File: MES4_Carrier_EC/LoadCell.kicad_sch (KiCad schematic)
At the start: 23 parts, among them J12 LC SIG, J13 LC EXC, U9 ADS1232IPWR

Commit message: Put relay coil feedback back on PA0-PA3 (MES4 GPIO standard)
All 14 module GPIOs now follow the MES4-CIF §2c table. The TCA9535 is
removed from the Relays 3-4 sheet and J1 fingers 43/45/47/49 drive the
relay 1-4 feedback dividers again. The winch relays are left undriven
(gate inputs no-connected, 100k pull-downs hold them off) until they
move to the TCA9535 + photoMOS design (HANDOFF.md step 2).

Removing U4 renumbers U5-U12 to U4-U11 and C15-C45 to C14-C44; the
README refs follow. Adds generator/checks.py (pin/pad, single-pin nets,
duplicate UUIDs, LCSC numbers), run by run.sh after ERC.

Co-Authored-By: Claude Opus 5.5 <noreply@anthropic.com>
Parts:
- removed C30: 100nF, Capacitor_SMD:C_0402_1005Metric, symbol Device:C
- removed R42: 100k, Resistor_SMD:R_0402_1005Metric, symbol Device:R
- removed U9: ADS1232IPWR, Package_SO:TSSOP-24_4.4x7.8mm_P0.65mm, symbol MES4-Carrier-EC:ADS1232IPW
- added C20: 10nF C0G, Capacitor_SMD:C_0402_1005Metric, symbol Device:C
- added R41: 100k, Resistor_SMD:R_0402_1005Metric, symbol Device:R
- added U8: ADS1232IPWR, Package_SO:TSSOP-24_4.4x7.8mm_P0.65mm, symbol MES4-Carrier-EC:ADS1232IPW
- C21, C24, C26: value 10nF C0G -> 100nF C0G; footprint Capacitor_SMD:C_0402_1005Metric -> Capacitor_SMD:C_1206_3216Metric; LCSC C3855387 -> C97946
- C22, C25: value 100nF C0G -> 10nF C0G; footprint Capacitor_SMD:C_1206_3216Metric -> Capacitor_SMD:C_0402_1005Metric; LCSC C97946 -> C3855387
- C27: value 100nF C0G -> 10uF 25V; footprint Capacitor_SMD:C_1206_3216Metric -> Capacitor_SMD:C_0805_2012Metric; LCSC C97946 -> C15850
- C28: value 10uF 25V -> 100nF; footprint Capacitor_SMD:C_0805_2012Metric -> Capacitor_SMD:C_0402_1005Metric; LCSC C15850 -> C1525
- renumbered R41 to R42
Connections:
- net +3V3_MOD: now also C29.1, U8.1 (DVDD), U8.19 (GAIN0), U8.20 (GAIN1)
- net GND: now also C22.2, C25.2, C27.2, C20.2, R41.2, U8.13 (AINN2), U8.14 (AINP2), U8.17 (AGND), U8.2 (DGND), U8.21 (SPEED), U8.3 (CLKIN/XTAL1), U8.5 (DGND), U8.6 (DGND), U8.7 (TEMP), U8.8 (A0); no longer C21.2, C24.2, C26.2
- net LC_AINN: now also C21.2, C22.1, U8.12 (AINN1); no longer C22.2, C23.1
- net LC_AINP: now also C20.1, U8.11 (AINP1); no longer C22.1
- net LC_CAPA: now also C26.1, U8.9 (CAP); no longer C27.1
- net LC_CAPB: now also C26.2, U8.10 (CAP); no longer C27.2
- net LC_DOUT: now also U8.24 (~{DRDY}/DOUT)
- net LC_EXC+: now also C27.1, U8.18 (AVDD); no longer C29.1
- net LC_REFN: now also C24.2, C25.1, U8.15 (REFN); no longer C25.2, C26.1
- net LC_REFP: now also C23.1, U8.16 (REFP); no longer C25.1
- net PA5: now also R41.1, U8.23 (SCLK); no longer R42.1
- net PA6: now also R42.1, U8.22 (~{PWDN})
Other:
- note added: "Signal and reference filters: 100 Ω per leg, 100 nF C0G across, 10 nF to GND (CIF §8a). The reference gets the same network so both time constants match (TI SBAS350 §8.2). REFP / REFN are sensed at J13 pins 1 / 2: route them as their own pair from the connector pads, not from the 5 V / GND planes. C26 = PGA bypass (pins 9-10)."
- note added: "U8 ADS1232 24-bit bridge ADC (TI SBAS350 weigh-scale configuration)"
- note removed: "Signal and reference filters: 100 Ω per leg, 100 nF C0G across, 10 nF to GND (CIF §8a). The reference gets the same network so both time constants match (TI SBAS350 §8.2). REFP / REFN are sensed at J13 pins 1 / 2: route them as their own pair from the connector pads, not from the 5 V / GND planes. C27 = PGA bypass (pins 9-10)."
- note removed: "U9 ADS1232 24-bit bridge ADC (TI SBAS350 weigh-scale configuration)"
- moved on the sheet: R42

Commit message: Drop relay coil feedback; winch on PA0/PA1, servo on USART2
User decision: free the four feedback pins instead of adding an I²C
expander. The Flasher template's 10k/15k/10 nF dividers are removed from
all relay channels and relay diagnosis is INA226-only. PA0/PA1 drive the
IM03GR winch relays again and PA2/PA3 carry the door servo UART
(USART2), so the SC16IS740 bridge, its crystal and caps, and the unused
TCA9535 code are removed. This deliberately differs from the MES4-CIF
§2c GPIO table; the GPIO map, root notes, README and HANDOFF say so.

189 parts, ERC clean, checks.py passes. README refs follow the
renumbering.

Co-Authored-By: Claude Opus 5.5 <noreply@anthropic.com>
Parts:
- removed C26: 100nF C0G, Capacitor_SMD:C_1206_3216Metric, symbol Device:C
- removed C27: 10uF 25V, Capacitor_SMD:C_0805_2012Metric, symbol Device:C
- removed C28, C29: 100nF, Capacitor_SMD:C_0402_1005Metric, symbol Device:C
- removed R36, R37, R38, R39, R40: 100Ω, Resistor_SMD:R_0402_1005Metric, symbol Device:R
- removed R41, R42: 100k, Resistor_SMD:R_0402_1005Metric, symbol Device:R
- added C16, C18, C19: 10nF C0G, Capacitor_SMD:C_0402_1005Metric, symbol Device:C
- added C17: 100nF C0G, Capacitor_SMD:C_1206_3216Metric, symbol Device:C
- added R28, R29, R30, R31, R32: 100Ω, Resistor_SMD:R_0402_1005Metric, symbol Device:R
- added R33, R34: 100k, Resistor_SMD:R_0402_1005Metric, symbol Device:R
- C20, C22: value 10nF C0G -> 100nF C0G; footprint Capacitor_SMD:C_0402_1005Metric -> Capacitor_SMD:C_1206_3216Metric; LCSC C3855387 -> C97946
- C21: value 100nF C0G -> 10nF C0G; footprint Capacitor_SMD:C_1206_3216Metric -> Capacitor_SMD:C_0402_1005Metric; LCSC C97946 -> C3855387
- C23: value 10nF C0G -> 10uF 25V; footprint Capacitor_SMD:C_0402_1005Metric -> Capacitor_SMD:C_0805_2012Metric; LCSC C3855387 -> C15850
- C24: value 100nF C0G -> 100nF; footprint Capacitor_SMD:C_1206_3216Metric -> Capacitor_SMD:C_0402_1005Metric; LCSC C97946 -> C1525
- C25: value 10nF C0G -> 100nF; LCSC C3855387 -> C1525
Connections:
- net +3V3_MOD: now also C25.1
- net GND: now also C21.2, C24.2, C16.2, C18.2, C19.2, R31.1, R33.2, R34.2; no longer C20.2, C22.2
- net LC_AINN: now also C17.2, C18.1, R29.2; no longer C21.2, C22.1
- net LC_AINP: now also C16.1, C17.1, R28.2; no longer C20.1, C21.1
- net LC_CAPA: now also C22.1
- net LC_CAPB: now also C22.2
- net LC_DOUT: now also R32.1
- net LC_EXC+: now also C23.1, C24.1, R30.1
- net LC_REFN: now also C20.2, C21.1, R31.2; no longer C24.2, C25.1
- net LC_REFP: now also C20.1, C19.1, R30.2; no longer C23.1, C24.1
- net LC_SIG+: now also R28.1
- net LC_SIG-: now also R29.1
- net PA4: now also R32.2
- net PA5: now also R33.1
- net PA6: now also R34.1
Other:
- note added: "Signal and reference filters: 100 Ω per leg, 100 nF C0G across, 10 nF to GND (CIF §8a). The reference gets the same network so both time constants match (TI SBAS350 §8.2). REFP / REFN are sensed at J13 pins 1 / 2: route them as their own pair from the connector pads, not from the 5 V / GND planes. C22 = PGA bypass (pins 9-10)."
- note removed: "Signal and reference filters: 100 Ω per leg, 100 nF C0G across, 10 nF to GND (CIF §8a). The reference gets the same network so both time constants match (TI SBAS350 §8.2). REFP / REFN are sensed at J13 pins 1 / 2: route them as their own pair from the connector pads, not from the 5 V / GND planes. C26 = PGA bypass (pins 9-10)."

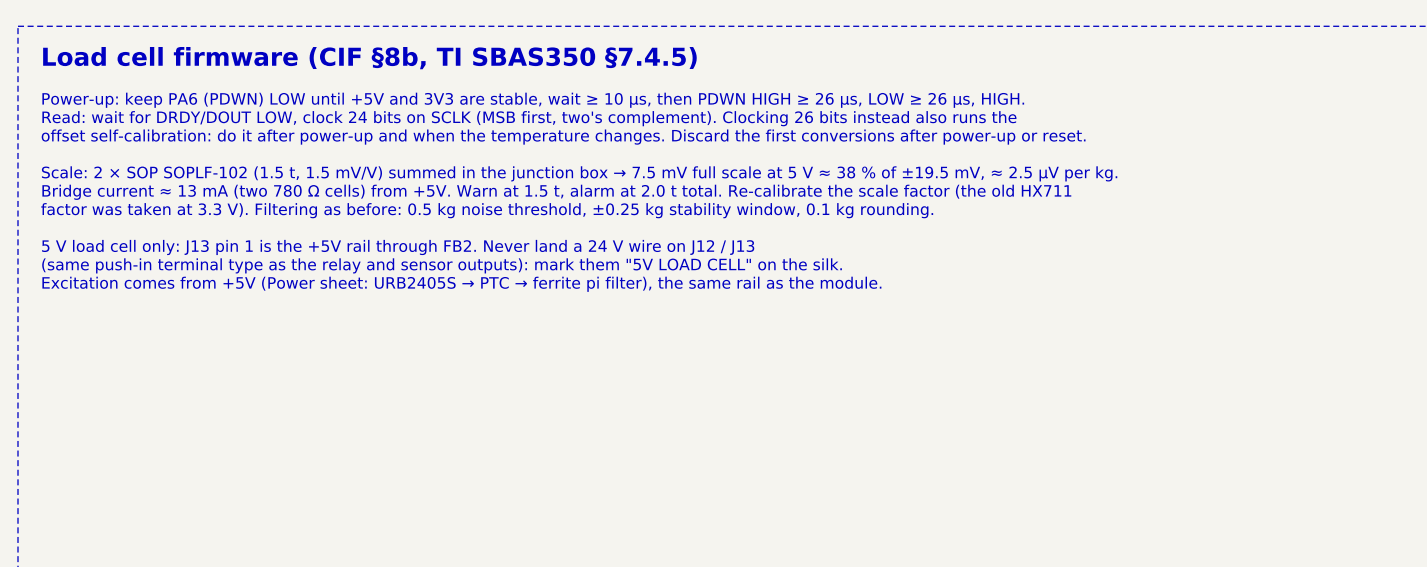
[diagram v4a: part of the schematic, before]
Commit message: Address design review R1: INA236, J15 polarity, review fixes
M1: U2-U5 are now TI INA236AIDDFR (C5443912, 50 V abs max, TSOT-23-8)
instead of the INA226 (40 V), since the SMBJ30A clamps at up to 48.4 V.
A project INA236 symbol keeps the INA226 body so the Flasher relay
wiring lands on the same pins; A1 and VBUS are gone (bus read on IN-),
addresses 0x40-0x43 via A0 = GND / VS / SDA / SCL. Same CONFIG / CAL /
MASK / ALERT values; notes give the 1.6 mV bus LSB and Device ID.
M3: J15 servo 24 V is pin 1 = +24 V like every power terminal.
L4: R38 servo RX series resistor 1k (limits PA3 back-feed).
L2: "current present" threshold 3 mA. L6: Power notes use 13 A / 2.2 W.
M2 / L5: silkscreen notes for "5V LOAD CELL - NEVER 24V" and
"CAN - NOT ETHERNET" (no keyed connector, by choice).
RJ45 1x4 footprint rebuilt from the HCTL drawing (14.0 mm ports,
Ø1.5 shield and Ø3.2 peg positions); U1 / U9 / U10 checked against the
JLC library and YLPTEC drawing. HANDOFF gains the review status table
and a layout checklist.

Co-Authored-By: Claude Opus 5.5 <noreply@anthropic.com>
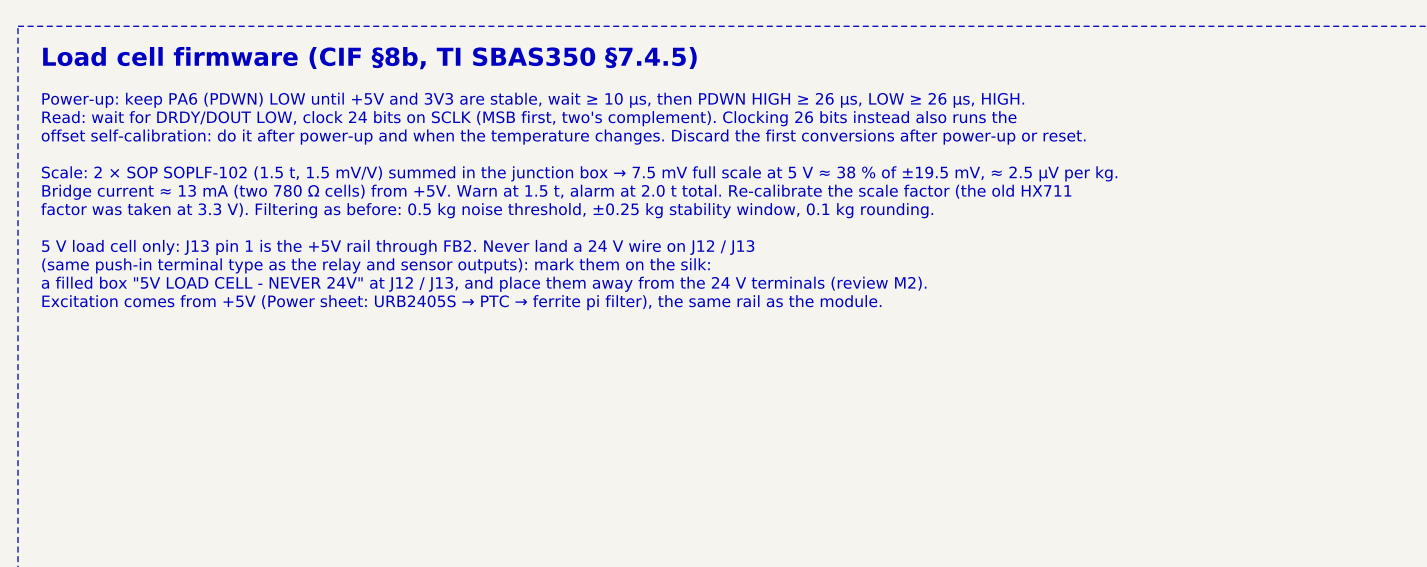
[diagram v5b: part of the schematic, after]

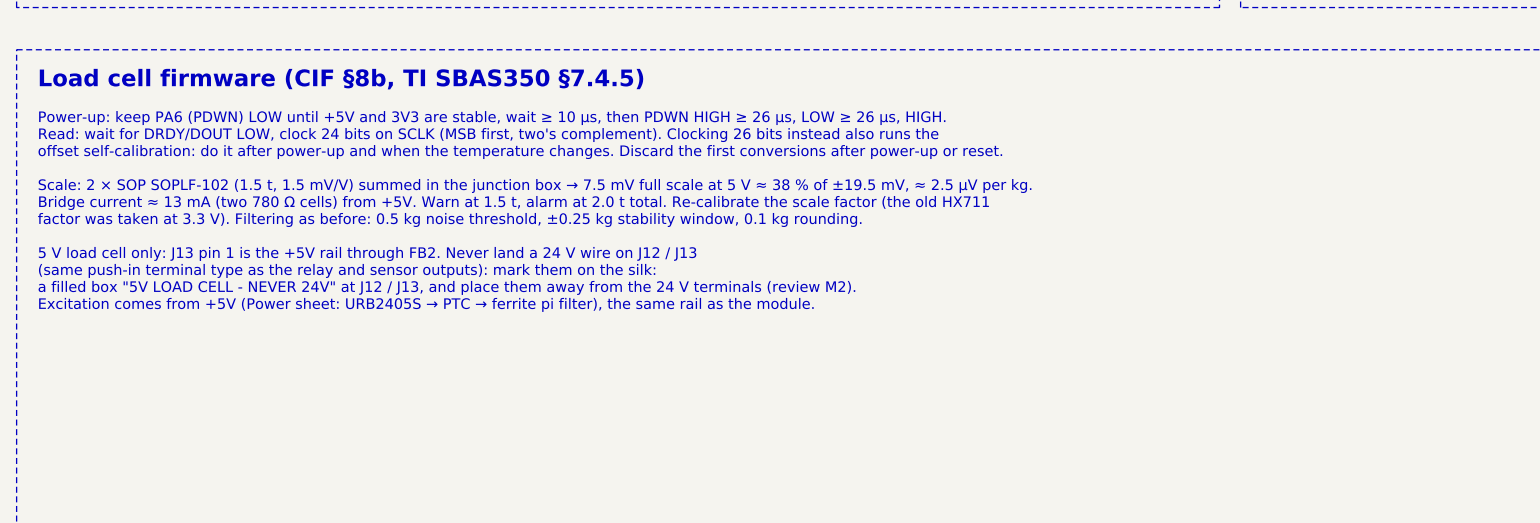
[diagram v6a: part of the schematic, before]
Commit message: Fix design review R3 findings: U9 part, stale LCSC fields, labels, J16
- B1: U9 is now YLPTEC URB2409S-6WR3 (C7468814, 9 V 6 W) on U1's
  footprint; the 10 W URB2409S-10WR3 isn't in JLC's assembly library.
  The production BOM had a 5 V module at U9 and the wrong SW2 because
  EasyEDA footprints carry an "LCSC Part" field the Fabrication Toolkit
  reads first: libs.py strips it (and the unprintable pin-1 dots it was
  copying back), and the new parts_sync.py syncs board footprints,
  values, fields and BOM flags from the schematic. TP1-TP9 and H2-H5
  are out of the BOM and CPL.
- M2 / L5: "5V LOAD CELL" across J12 / J13; "CANBUS" knockout by J4.
- B2: J16 moves 1.25 mm west so its mouth reaches the board edge.
- B8 / N6: README (one ground, U9, J16, labels, TPs), schematic notes
  and HANDOFF updated; 1:1 A4 print refreshed.
- DRC with parity at the 3 accepted J4 notes; nets, audit, DFM clean.
  production/ is stale until the Fabrication Toolkit is re-run.

Co-Authored-By: Claude Opus 5.5 <noreply@anthropic.com>
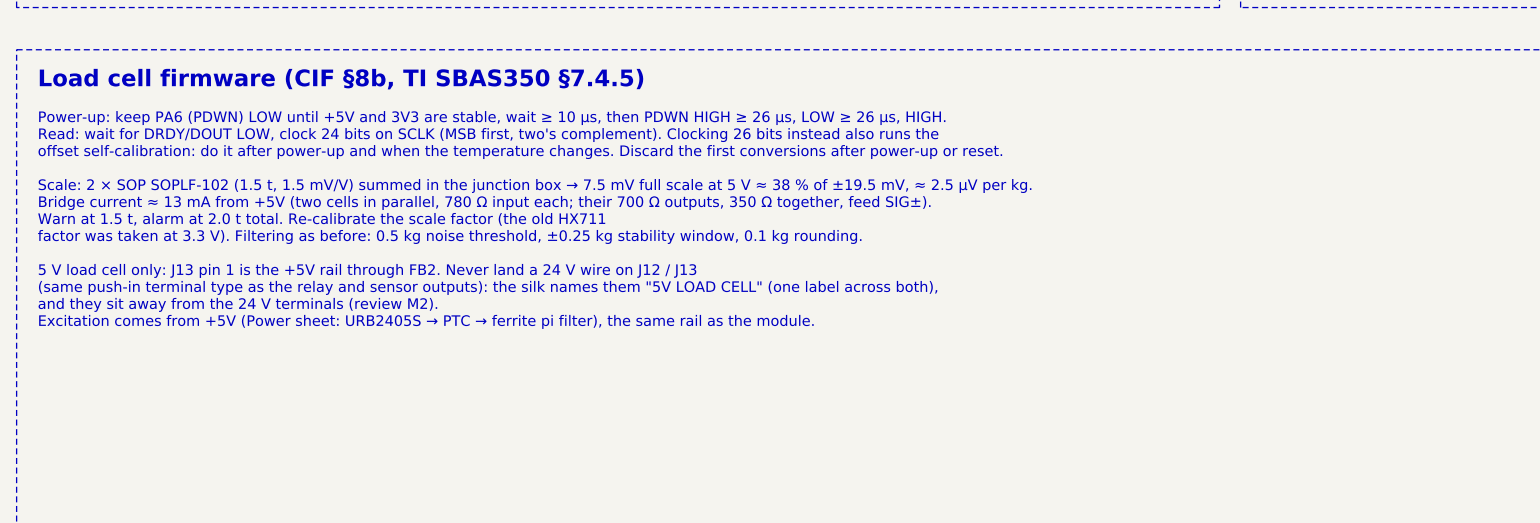
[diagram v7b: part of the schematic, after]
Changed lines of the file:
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@@
 		(effects (font (size 2 2) (bold yes)) (justify left top))
 	)
-	(text "Power-up: keep PA6 (PDWN) LOW until +5V and 3V3 are stable, wait ≥ 10 µs, then PDWN HIGH ≥ 26 µs, LOW ≥ 26 µs, HIGH.\nRead: wait for DRDY/DOUT LOW, clock 24 bits on SCLK (MSB first, two's complement). Clocking 26 bits instead also runs the\noffset self-calibration: do it after power-up and when the temperature changes. Discard the first conversions after power-up or reset.\n\nScale: 2 × SOP SOPLF-102 (1.5 t, 1.5 mV/V) summed in the junction box → 7.5 mV full scale at 5 V ≈ 38 % of ±19.5 mV, ≈ 2.5 µV per kg.\nBridge current ≈ 13 mA (two 780 Ω cells) from +5V. Warn at 1.5 t, alarm at 2.0 t total. Re-calibrate the scale factor (the old HX711\nfactor was taken at 3.3 V). Filtering as before: 0.5 kg noise threshold, ±0.25 kg stability window, 0.1 kg rounding.\n\n5 V load cell only: J13 pin 1 is the +5V rail through FB2. Never land a 24 V wire on J12 / J13\n(same push-in terminal type as the relay and sensor outputs): mark them on the silk:\na filled box \"5V LOAD CELL - NEVER 24V\" at J12 / J13, and place them away from the 24 V terminals (review M2).\nExcitation comes from +5V (Power sheet: URB2405S → PTC → ferrite pi filter), the same rail as the module."
+	(text "Power-up: keep PA6 (PDWN) LOW until +5V and 3V3 are stable, wait ≥ 10 µs, then PDWN HIGH ≥ 26 µs, LOW ≥ 26 µs, HIGH.\nRead: wait for DRDY/DOUT LOW, clock 24 bits on SCLK (MSB first, two's complement). Clocking 26 bits instead also runs the\noffset self-calibration: do it after power-up and when the temperature changes. Discard the first conversions after power-up or reset.\n\nScale: 2 × SOP SOPLF-102 (1.5 t, 1.5 mV/V) summed in the junction box → 7.5 mV full scale at 5 V ≈ 38 % of ±19.5 mV, ≈ 2.5 µV per kg.\nBridge current ≈ 13 mA from +5V (two cells in parallel, 780 Ω input each; their 700 Ω outputs, 350 Ω together, feed SIG±).\nWarn at 1.5 t, alarm at 2.0 t total. Re-calibrate the scale factor (the old HX711\nfactor was taken at 3.3 V). Filtering as before: 0.5 kg noise threshold, ±0.25 kg stability window, 0.1 kg rounding.\n\n5 V load cell only: J13 pin 1 is the +5V rail through FB2. Never land a 24 V wire on J12 / J13\n(same push-in terminal type as the relay and sensor outputs): the silk names them \"5V LOAD CELL\" (one label across both),\nand they sit away from the 24 V terminals (review M2).\nExcitation comes from +5V (Power sheet: URB2405S → PTC → ferrite pi filter), the same rail as the module."
 		(exclude_from_sim no)
 		(at 17.78 177.8 0)
